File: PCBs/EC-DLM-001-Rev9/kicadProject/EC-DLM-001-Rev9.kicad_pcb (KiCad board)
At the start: 2 copper layers, 145 x 75 mm, 88 parts, among them J1 DMX out, J10 RJ45, J11 RJ45, J12 BARREL_JACK, J13 5V, J14 3.3V, J15 DMX Test pins, J16 Aux LED Out 7-8, J17 Aux RST Out 7-8, J18 Aux ADC Input 7-8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

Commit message: TR04 + DLM01 REV9 adjustments.
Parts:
- removed C19: 10u, Capacitors_THT:CP_Radial_D6.3mm_P2.50mm
- removed C20, C23, C24, C7: 100n, Capacitors_SMD:C_0603_HandSoldering
- removed G***: LOGO, ec-dlm-001:LOGO-22mm
- removed J16: Aux LED Out 7-8, Pin_Headers:Pin_Header_Straight_1x02_Pitch2.54mm
- removed J17: Aux RST Out 7-8, Pin_Headers:Pin_Header_Straight_1x02_Pitch2.54mm
- removed J18: Aux ADC Input 7-8, Pin_Headers:Pin_Header_Straight_1x02_Pitch2.54mm
- removed J19: STrigger Input 7-8, Pin_Headers:Pin_Header_Straight_1x02_Pitch2.54mm
- removed J22: btn 6, Pin_Headers:Pin_Header_Straight_1x01_Pitch2.54mm
- removed J23: btn 3, Pin_Headers:Pin_Header_Straight_1x01_Pitch2.54mm
- removed J26: Micro_SD_Card, ec-dlm-001:Micro_SD_Card_Amphenol_114-00841-68
- removed R12, R15, R16, R26, R27: 10k, Resistors_SMD:R_0603_HandSoldering
- removed R22, R23: 220, Resistors_SMD:R_0603_HandSoldering
- removed R28, R29, R30: 27, Resistors_SMD:R_0603_HandSoldering
- removed REF** (x4): MountingHole_3.5mm, Mounting_Holes:MountingHole_3.5mm
- added F1: Fuse, Fuse_Holders_and_Fuses:Fuseholder5x20_horiz_open_lateral_Type-II, F.Cu at (78.0, 72.0)
- added L4: 10uH, Diodes_THT:D_DO-15_P12.70mm_Horizontal, F.Cu at (41.6, 81.2)
- added L5: 10uH, Diodes_THT:D_DO-15_P12.70mm_Horizontal, F.Cu at (42.2, 74.5)
- C4: value 100n -> 1000u; footprint Capacitors_SMD:C_0603_HandSoldering -> Capacitors_THT:CP_Radial_D14.0mm_P7.50mm
- J13: value 5V -> Bluetooth Module; footprint Pin_Headers:Pin_Header_Straight_1x02_Pitch2.54mm -> Pin_Headers:Pin_Header_Straight_1x06_Pitch2.54mm
- J20: value CONN_01X04 -> BTN-VDD
- L1: value Bead -> Fer Bead; footprint Inductors_SMD:L_0603_HandSoldering -> Diodes_THT:D_DO-15_P12.70mm_Horizontal
- moved C4 90.2 mm to (57.0, 92.7)
- moved C1 29.4 mm to (101.1, 84.2)
- moved J14 18.2 mm to (110.4, 101.7)
- moved C16 11.9 mm to (99.7, 99.0)
- moved L3 9.76 mm to (103.2, 100.6), turned to 90 degrees
- moved D3 9.21 mm to (111.6, 111.8)
- moved D4 9.21 mm to (104.1, 111.8)
- moved R14 9.10 mm to (104.2, 115.2)
- moved R2 9.02 mm to (90.3, 85.5)
- moved R6 9.02 mm to (90.3, 88.4)
- moved R3 9.02 mm to (90.3, 82.6)
- moved U1 8.49 mm to (89.8, 92.9)
- moved R13 8.41 mm to (111.6, 115.2)
- moved J13 7.34 mm to (81.1, 106.9), turned to 0 degrees
- moved C2 6.87 mm to (90.6, 100.3)
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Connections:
- net /LCDSDA renamed LCD_SDA
- net /PDIClk renamed PDI_CLK
- net /PDIData renamed PDI_DATA
- net /PE4 renamed ENCODER_B
- net Net-(D3-Pad2) renamed LED1
- net Net-(D4-Pad2) renamed LED2
- C1 pad 2: (no net) -> GND
- C3 pad 1: /PE3 -> ENCODER_MS
- C4 pad 1: /LCDSCL -> AVCC
- C4 pad 2: GND -> AnalogGND
- C8 pad 1: /PE5 -> ENCODER_A
- J10 pad 2: RST5 -> GND
- J10 pad 3: GND -> AnalogGND
- J10 pad 5: VCC -> L5_OUT_5
- J10 pad 6: STrig5 -> AVCC
- J10 pad 8: L5_OUT_5 -> VCC
- J11 pad 2: RST6 -> GND
- J11 pad 3: GND -> AnalogGND
- J11 pad 5: VCC -> L6_OUT_5
- J11 pad 6: STrig6 -> AVCC
- J11 pad 8: L6_OUT_5 -> VCC
- J12 pad 1: VCC -> Net-(F1-Pad2)
- J13 pad 1: GND -> (no net)
- J20 pad 3: VDD -> (no net)
- J20 pad 4: VDD -> (no net)
- J3 pad 4: /LCDSCL -> LCD_SCL
- J4 pad 2: VCC -> VDD
- J4 pad 3: /PE5 -> ENCODER_MS
- J4 pad 5: /PE3 -> ENCODER_A
- J6 pad 2: RST1 -> GND
- J6 pad 3: GND -> AnalogGND
- J6 pad 5: VCC -> L1_OUT_5
- J6 pad 6: STrig1 -> AVCC
- J6 pad 8: L1_OUT_5 -> VCC
- J7 pad 2: RST2 -> GND
- J7 pad 3: GND -> AnalogGND
- J7 pad 5: VCC -> L2_OUT_5
- J7 pad 6: STrig2 -> AVCC
- J7 pad 8: L2_OUT_5 -> VCC
- J8 pad 2: RST3 -> GND
- J8 pad 3: GND -> AnalogGND
- J8 pad 5: VCC -> L3_OUT_5
- J8 pad 6: STrig3 -> AVCC
- J8 pad 8: L3_OUT_5 -> VCC
- J9 pad 2: RST4 -> GND
- J9 pad 3: GND -> AnalogGND
- J9 pad 5: VCC -> L4_OUT_5
- J9 pad 6: STrig4 -> AVCC
- J9 pad 8: L4_OUT_5 -> VCC
- L1 pad 2: VDD -> AVCC
- U3 pad 12: Net-(J18-Pad1) -> (no net)
- U3 pad 13: Net-(J18-Pad2) -> (no net)
- U3 pad 16: STrig1 -> (no net)
- U3 pad 17: STrig2 -> (no net)
- U3 pad 18: STrig3 -> (no net)
- U3 pad 19: STrig4 -> (no net)
- U3 pad 20: STrig5 -> (no net)
- U3 pad 21: STrig6 -> BT_RX
- U3 pad 22: Net-(J19-Pad1) -> BT_TX
- U3 pad 23: Net-(J19-Pad2) -> (no net)
- U3 pad 26: BTN4 -> (no net)
- U3 pad 30: /PE5 -> ENCODER_MS
- U3 pad 33: BTN3 -> (no net)
- U3 pad 37: /LCDSCL -> LCD_SCL
- U3 pad 38: /PE3 -> ENCODER_A
- U3 pad 4: L7_OUT_3.3 -> (no net)
- U3 pad 40: SD_SS -> (no net)
- U3 pad 41: SD_MOSI -> (no net)
- U3 pad 42: SD_MISO -> (no net)
- U3 pad 43: SD_SCK -> (no net)
- U3 pad 46: RST6 -> (no net)
- U3 pad 47: RST5 -> (no net)
- U3 pad 48: RST4 -> (no net)
- U3 pad 49: RST3 -> (no net)
- U3 pad 5: L8_OUT_3.3 -> (no net)
- U3 pad 50: RST2 -> (no net)
- U3 pad 51: RST1 -> (no net)
- U3 pad 54: Net-(J17-Pad1) -> (no net)
- U3 pad 55: Net-(J17-Pad2) -> (no net)
- U5 pad 11: Net-(J16-Pad1) -> (no net)
- U5 pad 12: L8_OUT_3.3 -> (no net)
- U5 pad 8: Net-(J16-Pad2) -> (no net)
- U5 pad 9: L7_OUT_3.3 -> (no net)
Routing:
- net VDD: track 220.0 -> 0.00 mm, vias 4 -> 0
- net GND: track 156.6 -> 0.00 mm, vias 40 -> 0
- net RST3: track 113.2 -> 0.00 mm, vias 3 -> 0
- net SD_SS: track 86.7 -> 0.00 mm, vias 2 -> 0
- net RST6: track 78.0 -> 0.00 mm, vias 5 -> 0
- net STrig1: track 67.4 -> 0.00 mm, vias 2 -> 0
- net STrig2: track 66.3 -> 0.00 mm, vias 5 -> 0
- net SD_SCK: track 66.1 -> 0.00 mm, vias 2 -> 0
- net SD_MISO: track 62.4 -> 0.00 mm, vias 2 -> 0
- net DE-RE: track 60.7 -> 0.00 mm, vias 3 -> 0
- net L6_OUT_3.3: track 60.1 -> 0.00 mm, vias 2 -> 0
- net ADCTrig1: track 59.9 -> 0.00 mm, vias 2 -> 0
- net RST1: track 59.8 -> 0.00 mm, vias 2 -> 0
- net SD_MOSI: track 56.4 -> 0.00 mm, vias 4 -> 0
- net VDD-Filtered: track 54.6 -> 0.00 mm, vias 2 -> 0
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
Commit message: New Main board.
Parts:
- removed J14: 3.3V, Pin_Headers:Pin_Header_Straight_1x02_Pitch2.54mm
- removed L1: Fer Bead, Diodes_THT:D_DO-15_P12.70mm_Horizontal
- added C19: 100n, Capacitors_SMD:C_0805_HandSoldering, F.Cu at (119.9, 93.2)
- added C20: 68u, Capacitors_SMD:C_0805_HandSoldering, F.Cu at (120.9, 89.4)
- added C7: 39p, Capacitors_SMD:C_0805_HandSoldering, F.Cu at (107.7, 89.6)
- added D2: D_Schottky, Diodes_THT:D_A-405_P5.08mm_Vertical_AnodeUp, F.Cu at (109.4, 81.0)
- added R11: 200k, Resistors_SMD:R_0805_HandSoldering, F.Cu at (105.4, 89.6)
- added R12: 500, Resistors_SMD:R_0805_HandSoldering, F.Cu at (118.6, 89.5)
- added R5: 17.3k, Resistors_SMD:R_0805_HandSoldering, F.Cu at (111.9, 85.2)
- added R8: 150k, Resistors_SMD:R_0805_HandSoldering, F.Cu at (106.7, 85.2)
- added U6: LM2621, Housings_SSOP:VSSOP-8_3.0x3.0mm_Pitch0.65mm, F.Cu at (113.4, 89.4)
- C10, C11, C12, C13, C14, C18, C21, C22, C3, C6, C8, C9: footprint Capacitors_SMD:C_0603_HandSoldering -> Capacitors_SMD:C_0805_HandSoldering
- C17: footprint Capacitors_THT:CP_Radial_D14.0mm_P7.50mm -> Capacitors_THT:CP_Radial_D13.0mm_P5.00mm
- C4: value 1000u -> 22u; footprint Capacitors_THT:CP_Radial_D14.0mm_P7.50mm -> Capacitors_SMD:C_0805_HandSoldering
- L2, L3: footprint Inductors_SMD:L_0603_HandSoldering -> Inductors_SMD:L_0805_HandSoldering
- L4: value 10uH -> 6.8uH; footprint Diodes_THT:D_DO-15_P12.70mm_Horizontal -> Inductors_SMD:L_0805_HandSoldering
- L5: footprint Diodes_THT:D_DO-15_P12.70mm_Horizontal -> Inductors_SMD:L_0805_HandSoldering
- R1, R10, R17, R18, R24, R25, R4, R7, R9: footprint Resistors_SMD:R_0603_HandSoldering -> Resistors_SMD:R_0805_HandSoldering
- U1: footprint TO_SOT_Packages_THT:TO-220_Vertical -> TO_SOT_Packages_THT:TO-220-3_Vertical
- moved L4 75.6 mm to (117.1, 85.2)
- moved L5 72.4 mm to (112.1, 93.4)
- moved C4 49.7 mm to (106.7, 93.4)
- moved C1 28.9 mm to (87.3, 109.6)
- moved U5 11.7 mm to (128.9, 82.9)
- moved L2 6.33 mm to (156.7, 97.8)
- moved C13 1.92 mm to (144.6, 110.8), turned to 270 degrees
- moved J13 1.90 mm to (79.2, 107.0)
- moved C21 1.00 mm to (174.9, 99.3)
- moved C9 0.95 mm to (130.0, 98.5)
- moved C12 0.82 mm to (136.7, 110.8)
- moved C10 0.72 mm to (153.5, 102.4)
- moved R25 0.64 mm to (160.4, 98.9)
- moved C11 0.57 mm to (137.4, 87.1)
- moved R24 0.51 mm to (160.4, 96.8)
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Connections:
- C4 pad 1: AVCC -> VCC
- C4 pad 2: AnalogGND -> GND
- L4 pad 1: VCC -> Net-(D2-Pad2)
- L4 pad 2: Net-(L1-Pad1) -> VCC
- R3 pad 1: Net-(R2-Pad2) -> GND
- R3 pad 2: GND -> Net-(R2-Pad2)

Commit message: Revision board rev9
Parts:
- removed C20: 68u, Capacitors_SMD:C_0805_HandSoldering
- removed R12: 500, Resistors_SMD:R_0805_HandSoldering
- C19: value 100n -> 680u; footprint Capacitors_SMD:C_0805_HandSoldering -> Capacitors_THT:CP_Radial_D13.0mm_P7.50mm
- C4: value 22u -> 0.33u; footprint Capacitors_SMD:C_0805_HandSoldering -> Capacitors_THT:CP_Radial_D5.0mm_P2.50mm
- C7: value 39p -> 0.1u; footprint Capacitors_SMD:C_0805_HandSoldering -> Capacitors_THT:CP_Radial_D5.0mm_P2.50mm
- D2: value D_Schottky -> 1N5821; footprint Diodes_THT:D_A-405_P5.08mm_Vertical_AnodeUp -> TO_SOT_Packages_THT:TO-220-2_Vertical
- L4: value 6.8uH -> 100uH; footprint Inductors_SMD:L_0805_HandSoldering -> Inductors_THT:L_Radial_D9.5mm_P5.00mm_Fastron_07HVP
- L5: footprint Inductors_SMD:L_0805_HandSoldering -> Inductors_THT:L_Axial_L9.5mm_D4.0mm_P5.08mm_Vertical_Fastron_SMCC
- R11: value 200k -> 2k; footprint Resistors_SMD:R_0805_HandSoldering -> Resistors_THT:R_Axial_DIN0207_L6.3mm_D2.5mm_P10.16mm_Horizontal
- R5: footprint Resistors_SMD:R_0805_HandSoldering -> Resistors_THT:R_Axial_DIN0207_L6.3mm_D2.5mm_P10.16mm_Horizontal
- R8: value 150k -> 2.2k; footprint Resistors_SMD:R_0805_HandSoldering -> Resistors_THT:R_Axial_DIN0207_L6.3mm_D2.5mm_P10.16mm_Horizontal
- U6: value LM2621 -> LM2577; footprint Housings_SSOP:VSSOP-8_3.0x3.0mm_Pitch0.65mm -> TO_SOT_Packages_THT:TO-220-5_Vertical
- moved R13 73.6 mm to (185.1, 118.9)
- moved R14 73.6 mm to (177.7, 118.9)
- moved D3 73.0 mm to (184.5, 114.8)
- moved D4 73.0 mm to (177.0, 114.8)
- moved C5 39.8 mm to (123.3, 109.8)
- moved C16 33.4 mm to (131.3, 109.8)
- moved C2 27.4 mm to (116.3, 109.8), turned to 180 degrees
- moved L3 23.3 mm to (126.3, 103.8), turned to 0 degrees
- moved J20 21.1 mm to (166.8, 105.3)
- moved C1 19.5 mm to (95.3, 91.8), turned to 180 degrees
- moved R5 17.1 mm to (100.3, 97.8), turned to 0 degrees
- moved R2 15.1 mm to (92.3, 100.5)
- moved R3 15.1 mm to (92.3, 97.6)
- moved R6 15.1 mm to (92.3, 103.4)
- moved U1 15.0 mm to (91.3, 107.8)
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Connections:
- net Net-(F1-Pad2) renamed +5V
- C19 pad 1: Net-(C19-Pad1) -> AVCC
- C4 pad 1: VCC -> Net-(C4-Pad1)
- C7 pad 1: AVCC -> VCC
- C7 pad 2: Net-(C7-Pad2) -> GND
- R11 pad 1: Net-(C19-Pad1) -> Net-(R11-Pad1)
- R11 pad 2: Net-(R11-Pad2) -> GND
- R5 pad 1: Net-(C7-Pad2) -> Net-(R11-Pad1)
- R5 pad 2: GND -> AVCC
- R8 pad 1: AVCC -> Net-(R8-Pad1)
- R8 pad 2: Net-(C7-Pad2) -> Net-(C4-Pad1)
- U6 pad 1: GND -> Net-(R8-Pad1)
- U6 pad 2: Net-(C19-Pad1) -> Net-(R11-Pad1)
- U6 pad 3: Net-(R11-Pad2) -> GND
- U6 pad 4: Net-(C7-Pad2) -> Net-(D2-Pad2)
- U6 pad 5: GND -> VCC
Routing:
- added copper zone on F.Cu, net AVCC
- added copper zone on F.Cu, net VDD
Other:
- board text added: "LITDLM1-REV9"
- board text added: "LITIOO - LITDLM1 Designed by Kevin Isabelle Granby, Québec, Canada, 2019"
- board text removed: "EC-DLM-001-REV7"
- board text removed: "ELECTRO CASTLE Designed by Kevin Isabelle Granby, Québec, Canada, 2018"

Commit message: New board pour production
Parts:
- added ?: , ec-dlm-001:LOGO, F.Cu at (199.3, 96.2)
- added C20: 100n, Capacitors_THT:CP_Radial_D6.3mm_P2.50mm, F.Cu at (114.3, 106.2)
- added C23: 100n, Capacitors_THT:CP_Radial_D6.3mm_P2.50mm, F.Cu at (102.3, 102.8)
- added C24: 100n, Capacitors_THT:CP_Radial_D6.3mm_P2.50mm, F.Cu at (77.3, 109.8)
- added C25: 100n, Capacitors_THT:CP_Radial_D6.3mm_P2.50mm, F.Cu at (172.3, 77.8)
- added C26: 100n, Capacitors_THT:CP_Radial_D6.3mm_P2.50mm, F.Cu at (188.3, 77.8)
- added C27: 100n, Capacitors_THT:CP_Radial_D6.3mm_P2.50mm, F.Cu at (152.3, 77.8)
- added C28: 100n, Capacitors_THT:CP_Radial_D6.3mm_P2.50mm, F.Cu at (106.3, 76.8)
- added C29: 100n, Capacitors_THT:CP_Radial_D6.3mm_P2.50mm, F.Cu at (126.3, 77.8)
- added C30: 100n, Capacitors_THT:CP_Radial_D6.3mm_P2.50mm, F.Cu at (143.3, 77.8)
- added REF**: MountingHole_3.5mm, Mounting_Holes:MountingHole_3.5mm, F.Cu at (85.8, 123.0)
- added REF**: MountingHole_3.5mm, Mounting_Holes:MountingHole_3.5mm, F.Cu at (200.4, 123.0)
- added REF**: MountingHole_3.5mm, Mounting_Holes:MountingHole_3.5mm, F.Cu at (200.4, 68.8)
- added REF**: MountingHole_3.5mm, Mounting_Holes:MountingHole_3.5mm, F.Cu at (85.8, 68.8)
- C16, C2: value 10u -> 10u-tant
- moved L5 26.4 mm to (119.9, 77.0), turned to 180 degrees
- moved L4 18.8 mm to (121.3, 96.2)
- moved C19 10.4 mm to (117.3, 82.6), turned to 270 degrees
- moved L3 6.52 mm to (125.8, 110.3)
- moved D2 4.95 mm to (102.3, 82.8)
- moved U5 4.62 mm to (136.3, 79.8)
- moved C2 4.53 mm to (115.8, 114.3)
- moved C5 4.53 mm to (122.8, 114.3)
- moved C16 4.03 mm to (130.8, 113.8)
- moved C4 3.00 mm to (107.3, 102.8)
- moved U6 3.00 mm to (101.3, 87.8)
- moved U4 2.24 mm to (163.3, 81.8)
- moved F1 2.22 mm to (78.3, 74.2)
- moved R8 2.00 mm to (100.3, 91.8)
- moved J20 1.03 mm to (167.1, 106.3)
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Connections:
- D3 pad 1: Net-(D3-Pad1) -> LED1
- D3 pad 2: LED1 -> Net-(D3-Pad2)
- D4 pad 1: Net-(D4-Pad1) -> LED2
- D4 pad 2: LED2 -> Net-(D4-Pad2)
- R13 pad 1: Net-(D3-Pad1) -> Net-(D3-Pad2)
- R13 pad 2: GND -> VDD
- R14 pad 1: Net-(D4-Pad1) -> Net-(D4-Pad2)
- R14 pad 2: GND -> VDD
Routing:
- net AnalogGND: track 0.00 -> 261.3 mm, vias 0 -> 6
- net AVCC: track 0.00 -> 212.3 mm
- net LED1: track 0.00 -> 71.8 mm, vias 0 -> 3
- net ADCTrig1: track 0.00 -> 66.7 mm, vias 0 -> 3
- net VCC: track 0.00 -> 65.5 mm, vias 0 -> 1
- net BT_TX: track 0.00 -> 65.0 mm, vias 0 -> 4
- net GND: track 0.00 -> 64.9 mm, vias 0 -> 29
- net BT_RX: track 0.00 -> 63.1 mm, vias 0 -> 4
- net L1_OUT_5: track 0.00 -> 60.4 mm
- net LED2: track 0.00 -> 55.5 mm, vias 0 -> 2
- net ADCTrig2: track 0.00 -> 53.9 mm, vias 0 -> 3
- net DE-RE: track 0.00 -> 48.8 mm, vias 0 -> 4
- net ADCTrig6: track 0.00 -> 46.1 mm, vias 0 -> 3
- net RO: track 0.00 -> 44.4 mm, vias 0 -> 3
- net PDI_CLK: track 0.00 -> 44.0 mm, vias 0 -> 2
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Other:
- net class Xlarge added: clearance 0.2, trace_width 3, via_dia 1, via_drill 0.2
- board text added: "LITDLM1-REVISION9"
- board text removed: "LITDLM1-REV9"

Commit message: PCB Rouge
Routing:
- net BTN1: track 12.1 -> 13.0 mm
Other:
- net class Default: via_drill 0.2 -> 0.3
- net class Signal: via_drill 0.25 -> 0.3

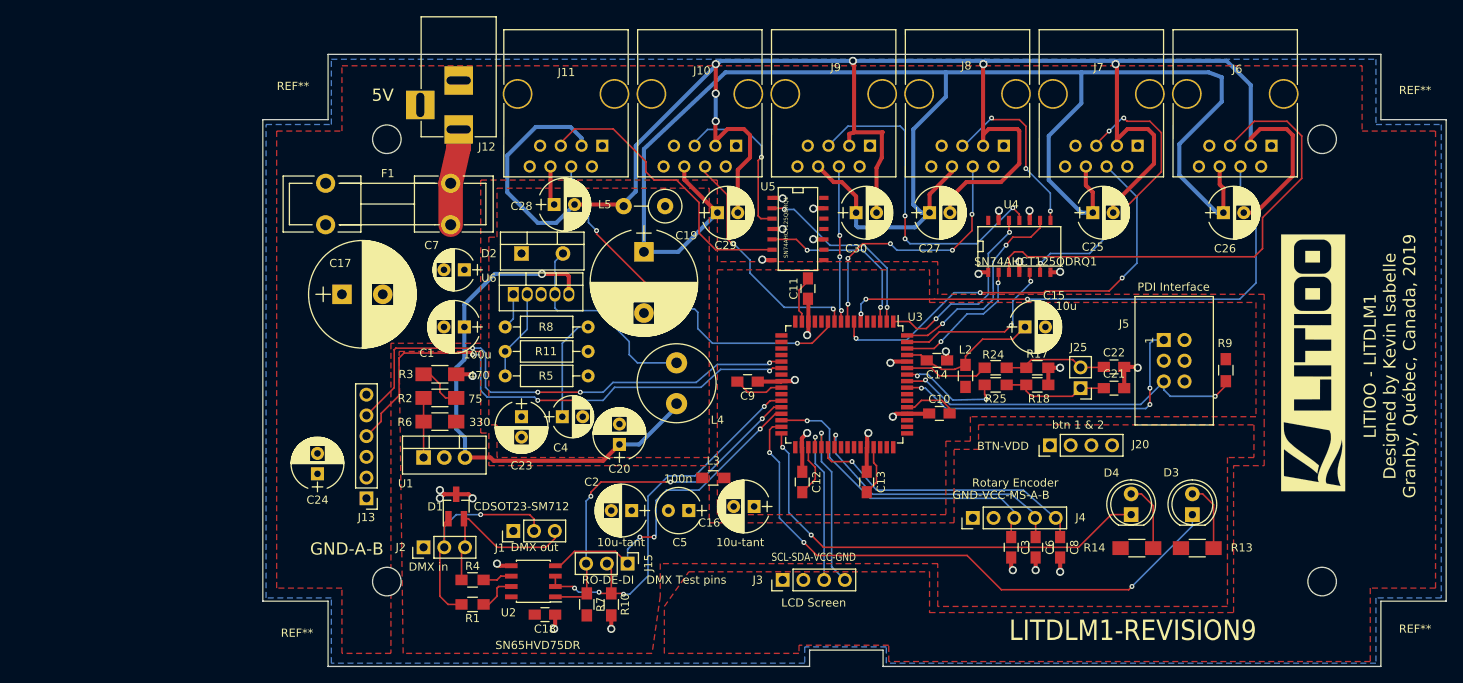
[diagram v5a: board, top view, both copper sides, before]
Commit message: Fixed screen corruption problem.
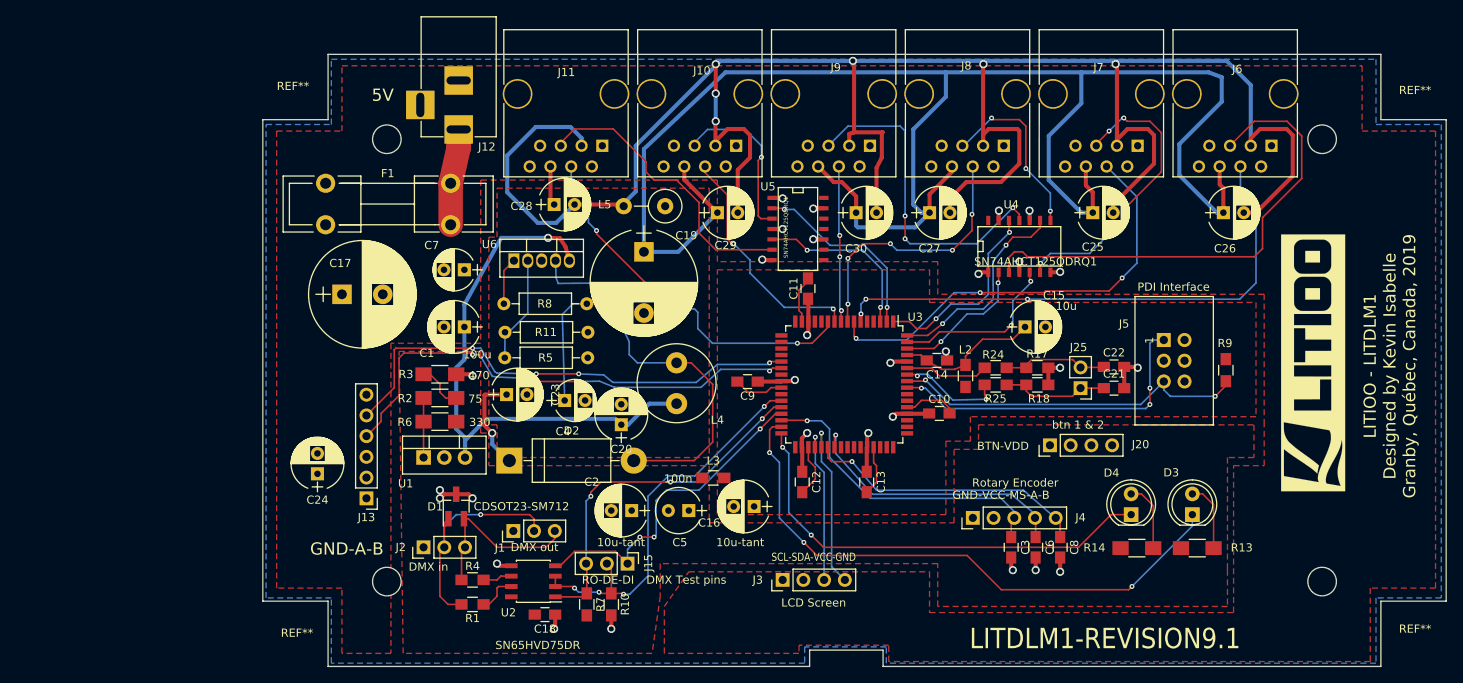
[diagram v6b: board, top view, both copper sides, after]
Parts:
- D2: footprint TO_SOT_Packages_THT:TO-220-2_Vertical -> Diodes_THT:D_DO-201AD_P15.24mm_Horizontal
- moved D2 25.4 mm to (100.8, 108.2)
- moved U6 4.12 mm to (101.4, 83.7)
- moved C23 3.27 mm to (100.5, 100.1), turned to 0 degrees
- moved R8 2.84 mm to (100.1, 89.0)
- moved C20 2.43 mm to (114.5, 103.8)
- moved R11 2.35 mm to (100.3, 92.5)
- moved R5 2.22 mm to (100.2, 95.6)
- moved C4 2.01 mm to (107.6, 100.8)
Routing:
- net Net-(D2-Pad2): track 25.8 -> 47.1 mm
- net AVCC: track 212.3 -> 224.4 mm, vias 0 -> 1
- net VCC: track 65.5 -> 70.0 mm
- net BT_TX: track 65.0 -> 61.2 mm
- net BT_RX: track 63.1 -> 60.0 mm
- net Net-(R11-Pad1): track 11.1 -> 13.3 mm
- net Net-(R8-Pad1): track 4.41 -> 5.79 mm
- net Net-(C4-Pad1): track 13.0 -> 14.1 mm
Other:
- board text added: "LITDLM1-REVISION9.1"
- board text removed: "LITDLM1-REVISION9"

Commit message: midi support
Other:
- net class Default removed
- net class Large removed
- net class Signal removed
- net class Xlarge removed
